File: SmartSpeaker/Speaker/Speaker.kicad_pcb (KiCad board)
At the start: 2 copper layers, 6.2 x 5.8 mm, 34 parts, among them J103 Screw_Terminal_01x02, J3 54-00166, Q1 DMG2305UX-13, U1 LM384, U2 LTC1655LCN8, U3 LM2675N-5, U4 LM4040LP-3

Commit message: PCB progress
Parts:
- moved C11 88.4 mm to (93.5, 35.6), turned to 90 degrees
- moved J103 82.5 mm to (175.3, 66.0), turned to 90 degrees
- moved D1 80.8 mm to (88.1, 43.7), turned to 90 degrees
- moved C3 78.0 mm to (134.4, 55.9), turned to 90 degrees
- moved TP4 61.2 mm to (71.4, 42.9)
- moved C12 58.5 mm to (103.4, 42.4)
- moved TP101 52.1 mm to (131.6, 78.5)
- moved TP6 40.8 mm to (136.1, 76.5)
- moved TP2 38.7 mm to (72.9, 60.2)
- moved TP5 38.4 mm to (152.4, 50.8)
- moved C6 35.6 mm to (83.8, 83.8)
- moved TP102 33.8 mm to (114.3, 75.6)
- moved C10 30.8 mm to (63.0, 86.9)
- moved C7 26.3 mm to (58.4, 71.1)
- moved C14 23.1 mm to (81.5, 50.2)
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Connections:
- net Net-(C5-Pad1) renamed /AudioOut
- net Net-(J103-Pin_1) renamed /SpeakerOut
- C11 pad 1: Net-(D1-K) -> /Power_converter/VSwitch
- D1 pad 1: Net-(D1-K) -> /Power_converter/VSwitch
- L1 pad 1: Net-(D1-K) -> /Power_converter/VSwitch
- L1 pad 2: /Power_converter/5VOut -> /Power_converter/VSwitch
- L1 pad 3: (no net) -> /Power_converter/VSwitch
- L1 pad 4: (no net) -> /Power_converter/VSwitch
- L1 pad 5: (no net) -> /Power_converter/5VOut
- L1 pad 6: (no net) -> /Power_converter/5VOut
- L1 pad 7: (no net) -> /Power_converter/5VOut
- L1 pad 8: (no net) -> /Power_converter/5VOut
- U3 pad 8: Net-(D1-K) -> /Power_converter/VSwitch
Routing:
- net /Power_converter/VoltageIn: track 18.9 -> 64.6 mm
- net /Power_converter/5VOut: track 0.00 -> 44.5 mm
- net Net-(U3-CB): track 0.00 -> 12.8 mm
- net Net-(U3-ON/~{OFF}): track 0.00 -> 6.43 mm
- net /Power_converter/VSwitch: track 0.00 -> 5.16 mm
- net Net-(U1-BYPASS): track 0.00 -> 5.08 mm
- net /SpeakerOut: track 0.00 -> 1.84 mm
- added copper zone on F.Cu, net /Power_converter/5VOut
- added copper zone on B.Cu, net /Power_converter/VSwitch
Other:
- board size 6.2 x 5.8 mm -> 147.3 x 121.9 mm

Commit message: PCB almost done
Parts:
- added J102: Screw_Terminal_01x03, TerminalBlock_Phoenix:TerminalBlock_Phoenix_PT-1,5-3-3.5-H_1x03_P3.50mm_Horizontal, F.Cu at (41.1, 77.5)
- moved C7 77.8 mm to (134.1, 53.3)
- moved C4 63.2 mm to (134.4, 83.8), turned to 180 degrees
- moved R1 59.5 mm to (137.9, 68.6), turned to -90 degrees
- moved TP1 57.2 mm to (90.4, 60.2)
- moved TP101 44.7 mm to (86.9, 76.7)
- moved Q1 43.6 mm to (55.1, 74.7), turned to 90 degrees
- moved A1 43.6 mm to (78.0, 96.0), turned to 90 degrees
- moved U4 43.4 mm to (69.6, 82.0)
- moved TP102 42.5 mm to (71.9, 77.2)
- moved R2 37.6 mm to (114.6, 58.9), turned to 180 degrees
- moved JP102 37.2 mm to (56.4, 82.5), turned to 90 degrees
- moved JP104 34.2 mm to (91.4, 55.1), turned to 0 degrees
- moved C10 32.8 mm to (91.2, 70.1), turned to 180 degrees
- moved C6 30.1 mm to (109.5, 68.1)
- moved JP103 29.2 mm to (64.0, 82.5), turned to 90 degrees
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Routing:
- net VDD: track 0.00 -> 60.0 mm
- net /Power_converter/5VOut: track 44.5 -> 103.7 mm
- net /Adafruit_1713_Microphone/OUTPUT: track 0.00 -> 55.3 mm
- net Net-(JP104-B): track 0.00 -> 43.7 mm
- net /AudioOut: track 0.00 -> 39.0 mm
- net Net-(U1--): track 0.00 -> 18.4 mm
- net Net-(U2-REF): track 0.00 -> 14.7 mm
- net Net-(A1-ADC_VREF): track 0.00 -> 12.1 mm
- net Net-(A1-VBUS): track 0.00 -> 11.5 mm, vias 0 -> 1
- net /SpeakerOut: track 1.84 -> 12.0 mm
- net Net-(JP101-B): track 0.00 -> 9.93 mm
- net Net-(A1-GP19): track 0.00 -> 9.72 mm
- net Net-(A1-GP18): track 0.00 -> 7.62 mm
- net Net-(A1-GP17): track 0.00 -> 7.62 mm
- net Net-(JP102-B): track 0.00 -> 4.62 mm, vias 0 -> 1
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
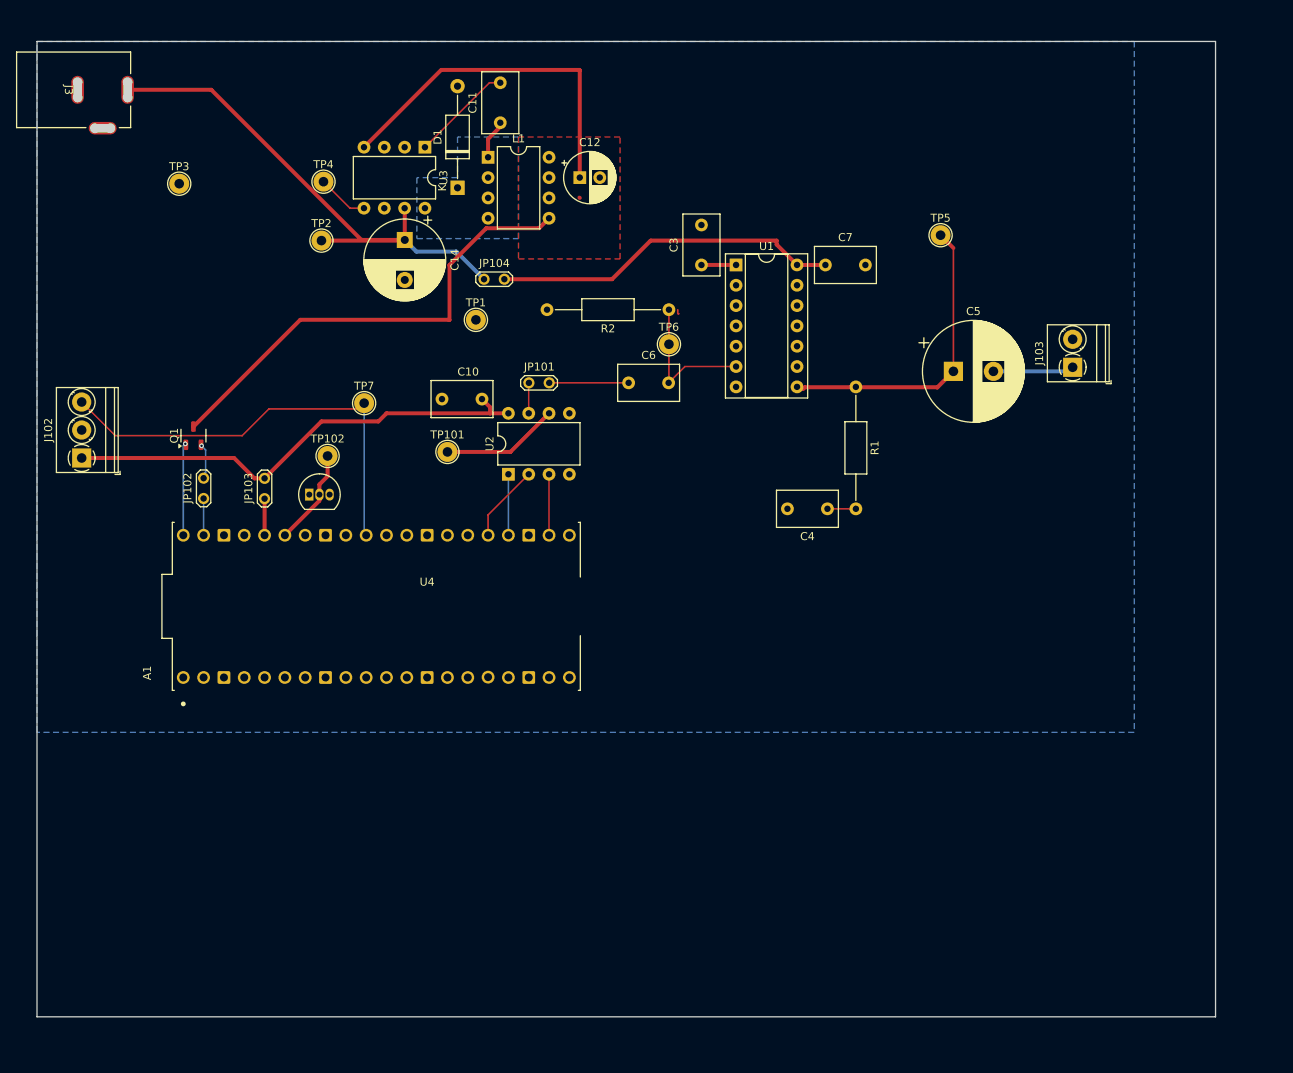
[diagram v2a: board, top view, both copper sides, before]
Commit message: overpower decoupling connections; TODO fix barrel jack
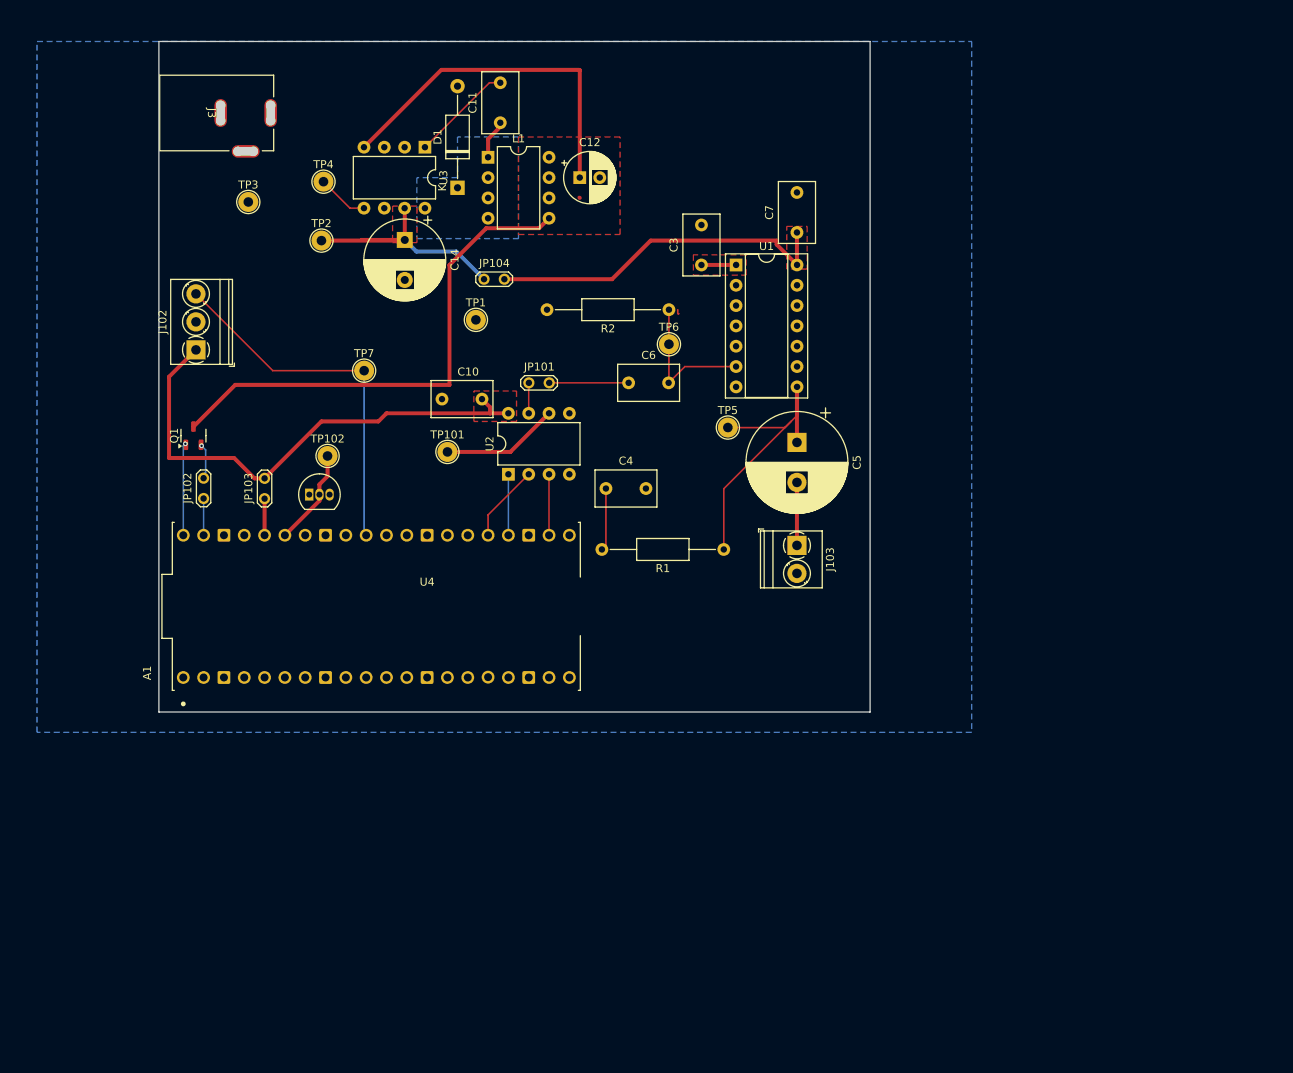
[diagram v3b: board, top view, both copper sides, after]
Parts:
- moved J103 41.0 mm to (130.6, 88.4), turned to -90 degrees
- moved TP5 35.8 mm to (121.9, 73.7)
- moved C4 27.8 mm to (106.7, 81.3), turned to 0 degrees
- moved R1 26.2 mm to (121.4, 88.9), turned to 180 degrees
- moved C5 21.5 mm to (130.6, 75.5), turned to -90 degrees
- moved J102 19.7 mm to (55.4, 64.0)
- moved J3 18.1 mm to (64.8, 34.3)
- moved TP3 8.93 mm to (62.0, 45.5)
- moved C7 5.40 mm to (130.6, 49.3), turned to 90 degrees
- moved TP7 4.06 mm to (76.5, 66.5)
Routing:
- net /Power_converter/VoltageIn: track 68.1 -> 31.8 mm
- net /Adafruit_1713_Microphone/OUTPUT: track 55.3 -> 45.7 mm
- net /Power_converter/5VOut: track 103.7 -> 108.5 mm
- net Net-(C4-Pad1): track 3.56 -> 7.83 mm
- net /SpeakerOut: track 12.0 -> 7.87 mm
- net VDD: track 60.0 -> 63.9 mm
- net /AudioOut: track 39.0 -> 40.3 mm
- net Net-(JP104-B): track 43.7 -> 44.2 mm
- added copper zone on F.Cu, net /Power_converter/VoltageIn
- added copper zone on F.Cu, net Net-(JP104-B)
- added copper zone on F.Cu, net Net-(U1-BYPASS)
- added copper zone on F.Cu, net VDD
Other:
- board size 147.3 x 121.9 mm -> 88.9 x 83.8 mm

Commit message: add potentiometer, prepare to make traces wider
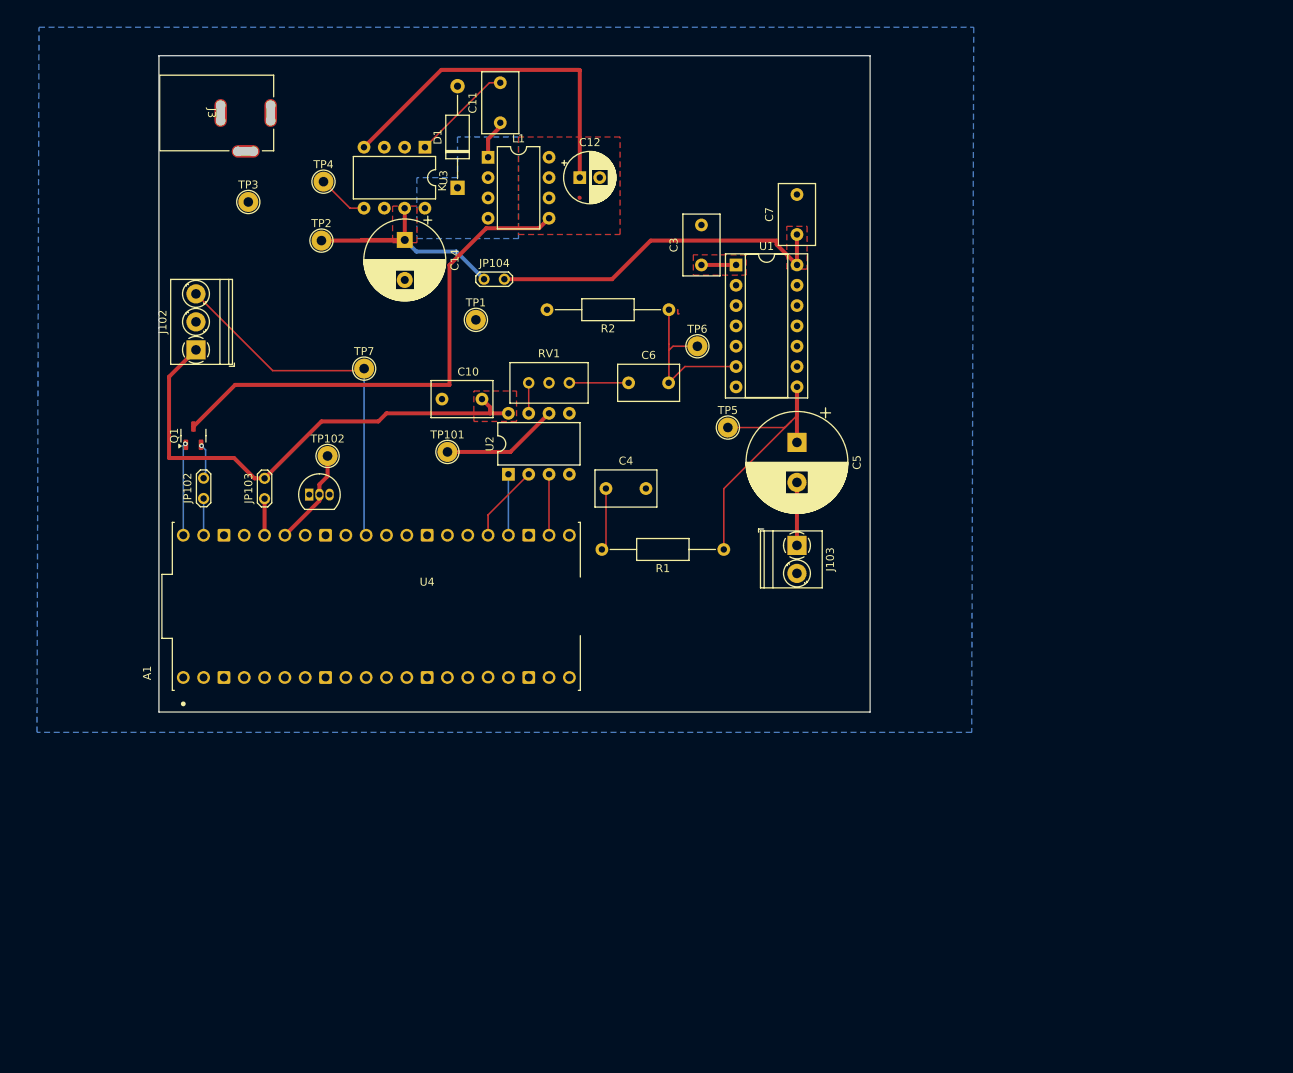
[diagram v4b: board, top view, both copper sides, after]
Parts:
- removed JP101: Jumper_2_Bridged, TestPoint:TestPoint_2Pads_Pitch2.54mm_Drill0.8mm
- added RV1: R_Potentiometer_Trim, Potentiometer_THT:Potentiometer_Bourns_3296W_Vertical, F.Cu at (102.1, 68.1)
- moved TP6 3.57 mm to (118.1, 63.5)
- moved TP7 0.25 mm to (76.5, 66.3)
- moved C7 0.25 mm to (130.6, 49.5)
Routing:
- net Net-(U1--): track 18.4 -> 22.2 mm
- net Net-(C6-Pad1): track 9.93 -> 7.41 mm
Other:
- board size 88.9 x 83.8 mm -> 88.9 x 82 mm

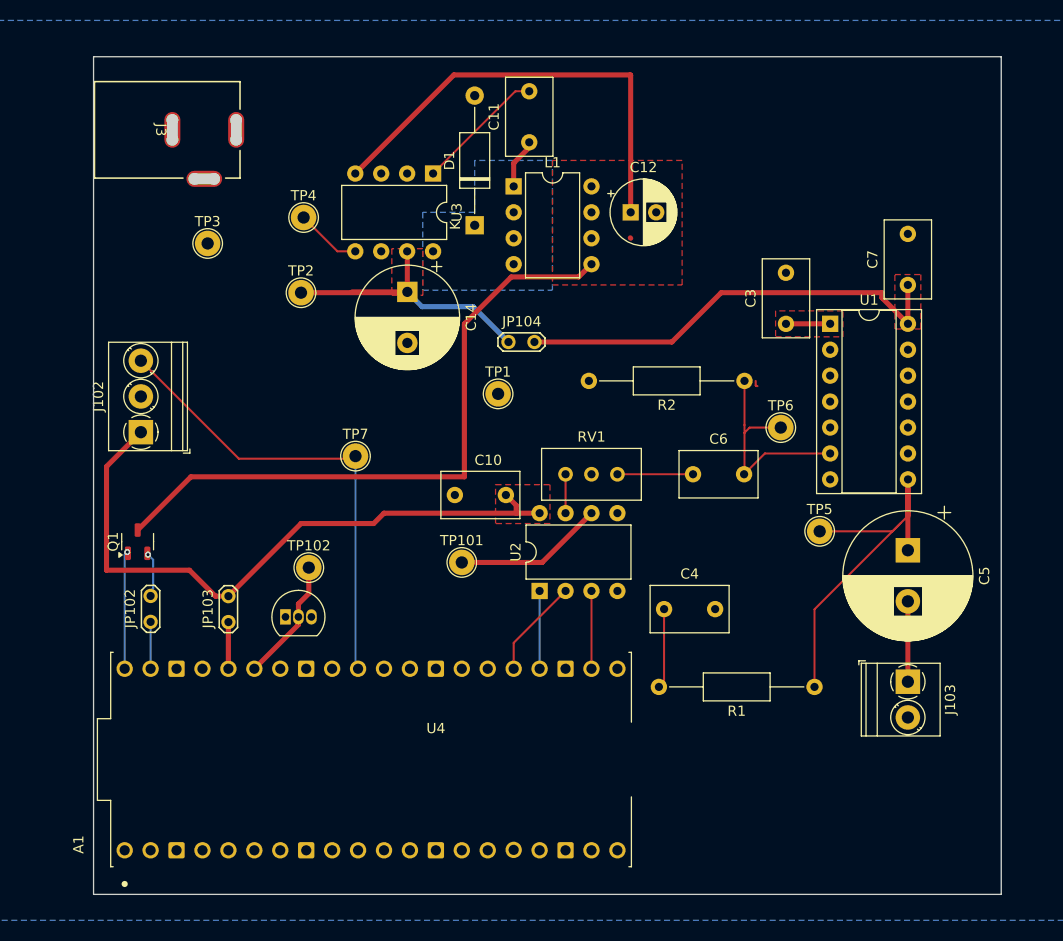
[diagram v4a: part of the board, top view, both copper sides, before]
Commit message: widen traces
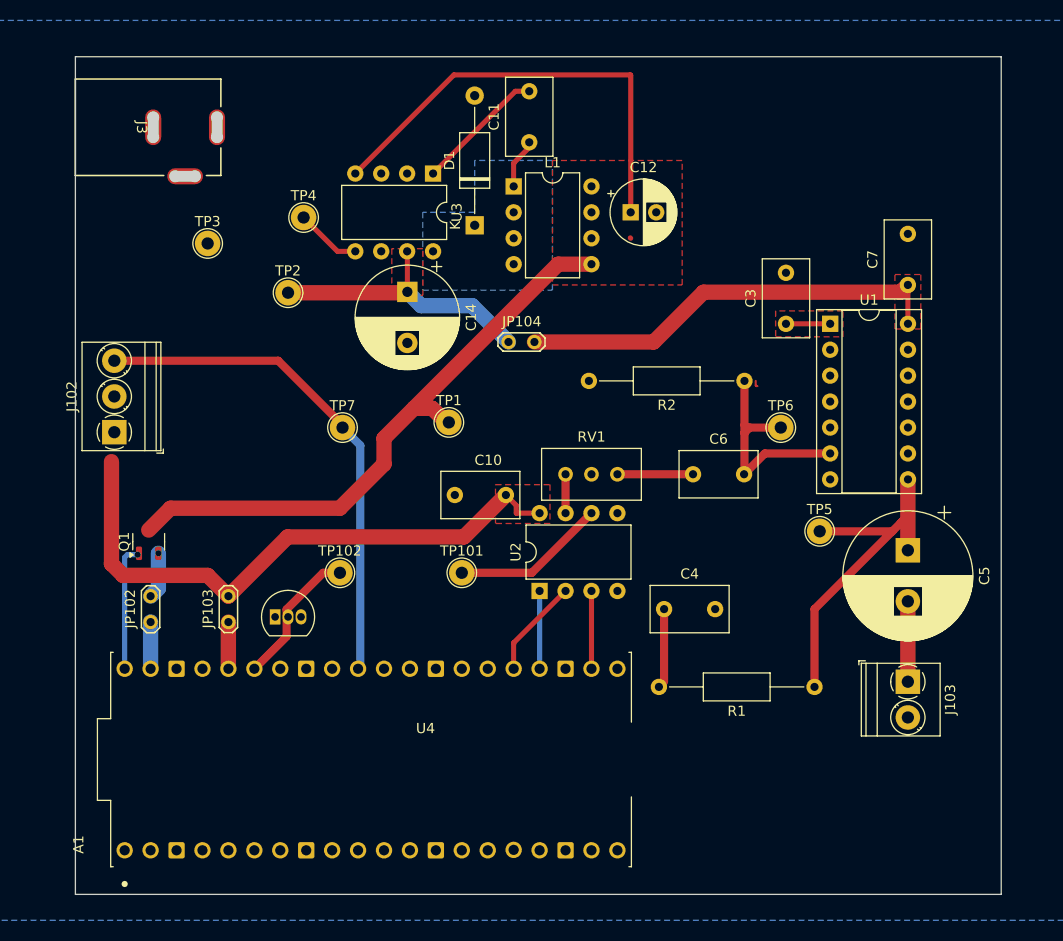
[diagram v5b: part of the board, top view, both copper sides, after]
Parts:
- moved TP1 5.58 mm to (85.6, 63.0)
- moved TP102 3.09 mm to (74.9, 77.7)
- moved TP7 3.07 mm to (75.2, 63.5)
- moved J102 2.60 mm to (52.8, 64.0)
- moved J3 1.90 mm to (62.9, 34.1)
- moved TP2 1.27 mm to (69.8, 50.3)
- moved Q1 1.08 mm to (56.2, 74.7)
- moved TP101 1.02 mm to (86.9, 77.7)
- moved U4 1.02 mm to (68.6, 82.0)
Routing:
- net /Power_converter/VoltageIn: track 31.8 -> 26.4 mm
- net VDD: track 63.9 -> 58.5 mm
- net /Power_converter/5VOut: track 108.5 -> 104.1 mm
- net /Adafruit_1713_Microphone/OUTPUT: track 45.7 -> 50.0 mm
- net /AudioOut: track 40.3 -> 38.4 mm
- net Net-(A1-ADC_VREF): track 12.1 -> 13.8 mm
- net Net-(JP104-B): track 44.2 -> 43.0 mm
- net Net-(U2-REF): track 14.7 -> 15.8 mm
- net Net-(A1-VBUS): track 11.5 -> 12.3 mm
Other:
- board size 88.9 x 82 mm -> 90.7 x 82 mm
